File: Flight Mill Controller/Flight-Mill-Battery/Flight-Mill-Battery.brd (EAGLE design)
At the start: 121.9 x 120 mm, 219 parts, among them IC1 STM32G0B1RET6, IC10 SN65HVD3082EDR, IC11 TPS54202DDCR, IC12 LD117AS50TR, IC13 LD117AS33TR, IC2 CSTNE8M00G520000R0, IC3 MCP6001UT, IC4 LMV641, IC5 LMV641, IC6 LMV641, IC7 LMV641, IC8 LMV641, IC9 LMV641, J1 1050170001, J2 61300411121, J3 615008148521, J4 61300411121, K1 RYA31012, K2 RYA31012, Q1 BC817, Q2 UT2955G-AA3-R, Q3 2N7002, Q4 UT2955G-AA3-R, Q5 2N7002, Q6 UT2955G-AA3-R, Q7 2N7002, Q8 UT2955G-AA3-R, Q9 2N7002, X1 B2B-XH-AM(LF)(SN), X10 726386-2TE_726386-2, X11 726386-2TE_726386-2, X12 726386-2TE_726386-2, X13 726386-2TE_726386-2, X14 726386-2TE_726386-2, X15 726386-2TE_726386-2, X17 282834-3, X18 282834-3, X2 B2B-XH-AM(LF)(SN), X23 282834-2, X24 282834-3, X3 WF2549-2WS05S0B01, X4 282834-2, X5 726386-2TE_726386-2, X6 282834-2, X7 726386-2TE_726386-2, X8 5-102203-3, X9 5-102203-3

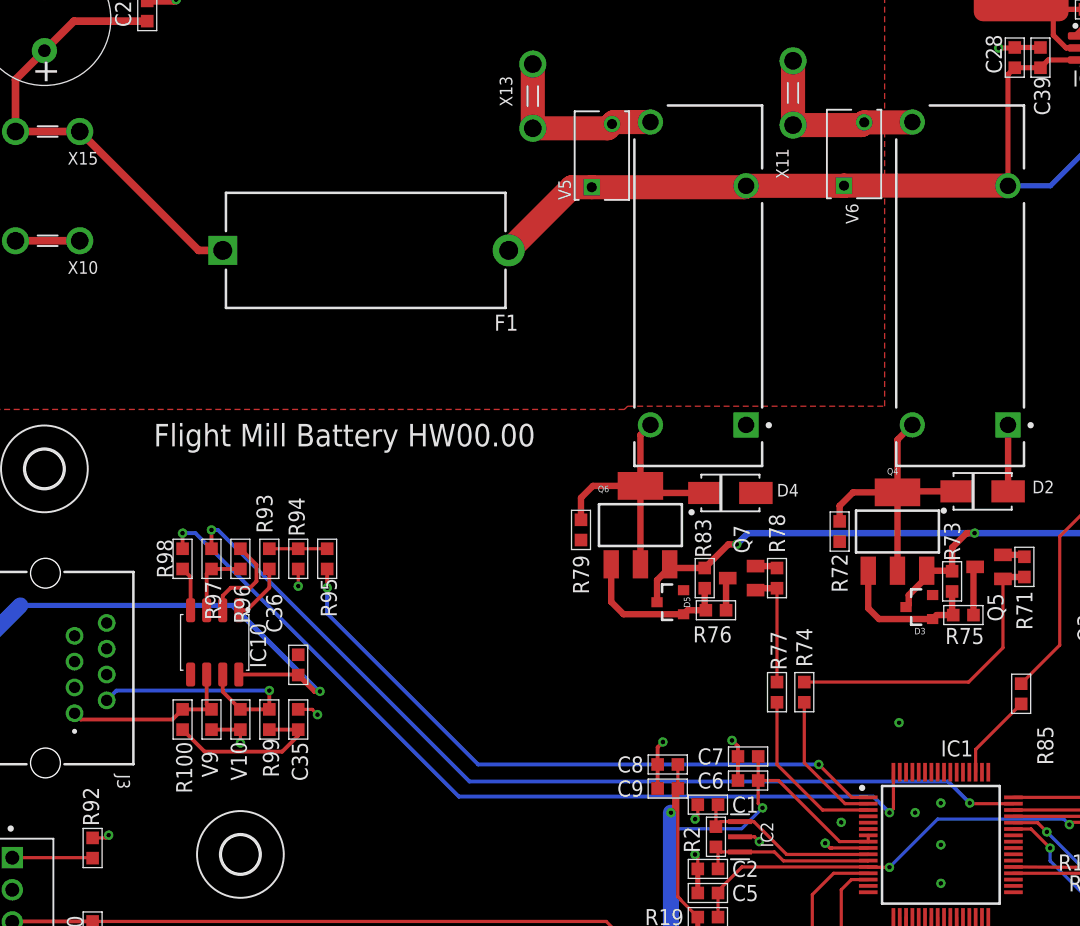
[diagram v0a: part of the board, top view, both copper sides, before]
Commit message: HW00.00 Ongoing
Added Coin battery and 32KHz Crystal for RTC retention
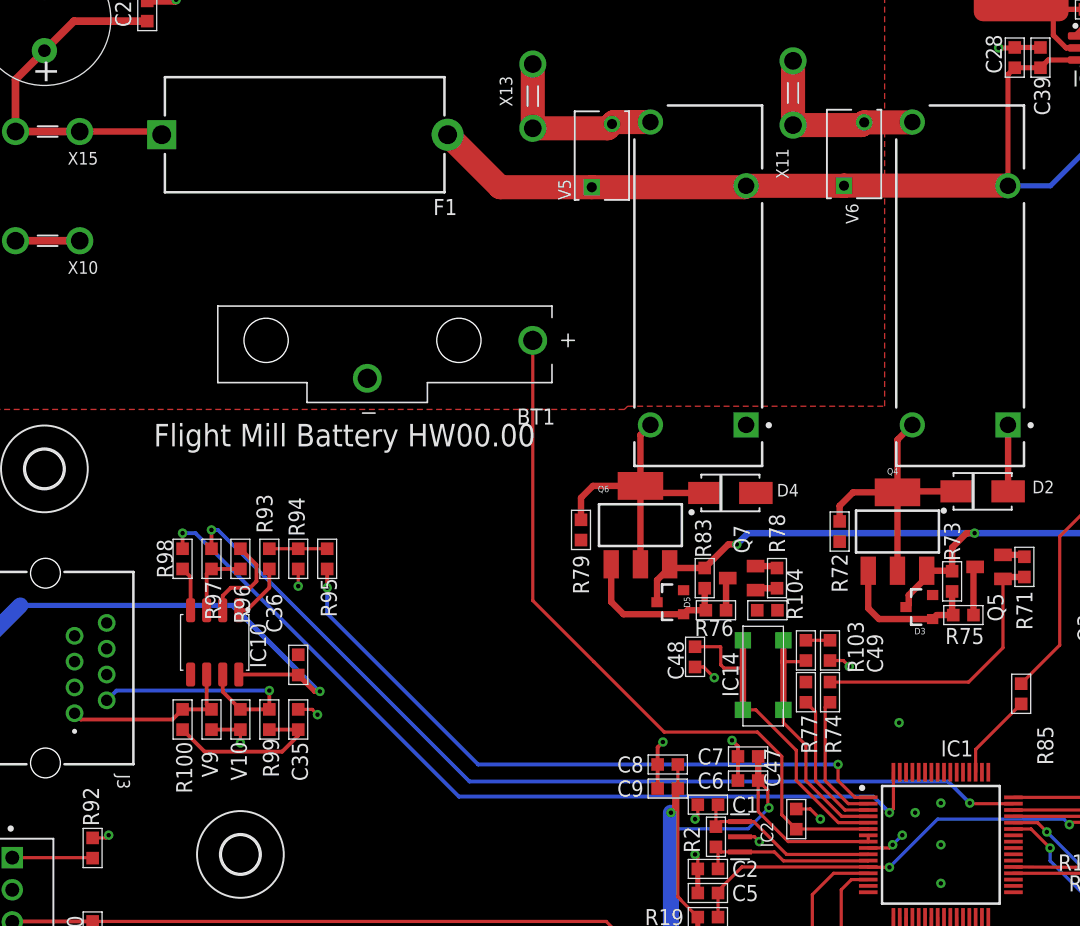
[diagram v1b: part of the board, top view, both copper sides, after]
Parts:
- added BT1: 1065, Labops_Lib_AH:BAT_1065
- added C47: 100nF/50V, Labops_Lib_AH:EIA0603
- added C48, C49: 10pF/50V, Labops_Lib_AH:EIA0603
- added IC14: G43270019, Labops_Lib_AH:G43270019
- added R103: 0R 1%, Labops_Lib_AH:EIA0603
- added R104: 22k 1%, Labops_Lib_AH:EIA0603
- R2: value 10K 1% -> n.P
- moved F1 10.3 mm to (27.2, 95.5)
- moved R77 2.29 mm to (66.8, 51.4)
- moved R74 2.03 mm to (68.7, 51.4)
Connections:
- new net N$65: BT1.P, C47.1, IC1.6
- new net N$67: C48.1, IC1.5, IC14.3, IC14.4, R104.2
- new net N$69: IC1.4, IC14.1, IC14.2, R103.1, R104.1
- new net N$72: C49.1, R103.2
- net GND: now also BT1.N, C47.2, C48.2, C49.2
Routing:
- net N$65: track 0.00 -> 57.3 mm
- net N$67: track 0.00 -> 25.9 mm
- net N$69: track 0.00 -> 19.7 mm
- net V24V0_B4_FUSE: track 36.7 -> 28.1 mm
- net N$46: track 9.17 -> 1.76 mm
- net GND: track 251.5 -> 256.9 mm, vias 79 -> 82
- net V24V0: track 75.1 -> 79.6 mm
- net V3V3: track 348.1 -> 350.2 mm
- net N$43: track 24.8 -> 22.7 mm
- net DO_HUMIDIFIER_ON: track 13.6 -> 11.6 mm
- net N$72: track 0.00 -> 1.91 mm
- net DI_USART_RX: track 52.3 -> 53.1 mm
- net DO_HEATER_ON: track 11.2 -> 10.5 mm

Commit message: HW01
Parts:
- removed C20, C21: 100nF/50V, Labops_Lib_AH:EIA0603
- removed IC9: LMV641, Labops_Lib_AH:SOT-23-5
- removed R103, R44, R58: 0R 1%, Labops_Lib_AH:EIA0603
- removed R43, R56, R57: 100R 1%, Labops_Lib_AH:EIA0603
- removed R54, R55: 1.5K 1%, Labops_Lib_AH:EIA0603
- added C50, C51, C52: 100nF/50V, Labops_Lib_AH:EIA0603
- added IC15: LMV641, Labops_Lib_AH:SOT-23-5
- added R105: 10R 1%, Labops_Lib_AH:EIA0603
- added R106, R107: 2.49K 1%, Labops_Lib_AH:EIA0603
- C11, C17: value 100nF/50V -> 0R 1%
- C15, C19: value 100nF/50V -> 10pF/50V
- C25: value (none) -> 100nF
- C35: value 100nF 100V -> 100pF 100V
- R14: value 47K 1% -> 100K 1%
- R22, R84: value 10k 1% -> 100R 1%
- R33, R34: value 10K 1% -> 100R 1%
- R39, R53: value 10K 1% -> n.P
- R40: value 1.5K 1% -> 10R 1%
- R41: value 100R 1% -> 2.49KK 1%
- R42: value 1.5K 1% -> 2.49K 1%
- R52: value 10K 1% -> 10k 1%
- R9: value 330R 1% -> 33R 1%
- moved C19 61.5 mm to (59.1, 50.0), turned to 180 degrees
- moved C15 46.6 mm to (66.8, 54.7), turned to 90 degrees
- moved R41 7.78 mm to (26.8, 17.0), turned to 270 degrees
- moved R42 7.67 mm to (28.6, 17.0), turned to 270 degrees
- moved R40 5.75 mm to (27.6, 26.3), turned to 0 degrees
- moved IC6 5.59 mm to (27.7, 22.7), turned to 90 degrees
- moved R39 3.58 mm to (30.4, 17.0)
- moved C13 3.56 mm to (25.0, 17.0)
- moved C48 1.67 mm to (58.3, 52.6), turned to 90 degrees
- moved R38 1.40 mm to (32.1, 17.0)
- moved C14 1.09 mm to (24.9, 22.7), turned to 90 degrees
- moved C49 0.64 mm to (69.3, 54.7)
- moved R74 0.64 mm to (69.3, 51.4)
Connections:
- removed net N$22: IC6.1, R44.2
- removed net N$28: IC9.3, R57.2
- removed net N$29: IC9.4, R56.2
- removed net N$30: C20.1, R55.2, R56.1
- removed net N$31: IC9.1, R58.2
- removed net VREF_O2: IC4.3, IC7.3, R31.2, R32.1, R36.2, R42.1, R45.2, R46.1, R50.2, R55.1
- new net N$70: IC15.4, R105.2
- new net N$71: IC15.1, R105.1, R50.2
- new net VREF_O2_1: C51.2, IC7.3, R45.2, R46.1
- new net VREF_O2_2: IC4.3, R31.2, R32.1
- net AI_O2_SENSOR: no longer R40.1
- net AI_O2_SENSOR1: no longer R44.1
- net AI_O2_SENSOR2: no longer R58.1
- net GND: now also C14.1, C50.2, C51.1, C52.1, IC10.5, IC15.2, R106.2, R41.2; no longer C14.2, C15.2, C19.1, C20.2, C21.2, IC9.2
- net N$15: now also IC6.4; no longer C13.2, R41.1
- net N$18: now also IC6.1, R36.2, R40.1; no longer IC6.3, R41.2
- net N$20: now also C19.2, C48.1; no longer IC6.4, R43.2
- net N$21: now also C13.2, IC6.3, R41.1, R42.1; no longer C14.1, R42.2, R43.1
- net N$27: now also C52.2, IC15.3, R106.1, R107.1; no longer C19.2, R54.2, R57.1
- net N$32: no longer R54.1
- net N$67: now also C19.1; no longer C48.1
- net N$69: now also C15.1; no longer R103.1
- net N$72: now also C15.2; no longer R103.2
- net V5V0: now also C14.2, C50.1, IC15.5, R107.2, R42.2; no longer C15.1, C21.1, IC9.5
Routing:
- net VREF_O2: track 104.9 -> 0.00 mm, vias 6 -> 0
- net V5V0: track 461.2 -> 499.0 mm, vias 12 -> 10
- net N$71: track 0.00 -> 26.1 mm
- net N$18: track 5.17 -> 23.4 mm, vias 0 -> 2
- net VREF_O2_2: track 0.00 -> 11.5 mm
- net VREF_O2_1: track 0.00 -> 11.2 mm
- net N$46: track 1.76 -> 12.4 mm, vias 0 -> 2
- net GND: track 256.9 -> 263.9 mm, vias 82 -> 95
- net AI_O2_SENSOR: track 15.3 -> 8.43 mm
- net N$28: track 5.92 -> 0.00 mm
- net N$30: track 4.32 -> 0.00 mm
- net N$21: track 3.48 -> 7.56 mm
- net N$31: track 3.91 -> 0.00 mm
- net N$29: track 2.82 -> 0.00 mm
- net N$69: track 19.7 -> 22.2 mm
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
